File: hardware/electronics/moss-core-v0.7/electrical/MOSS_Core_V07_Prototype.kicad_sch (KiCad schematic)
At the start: 0 parts

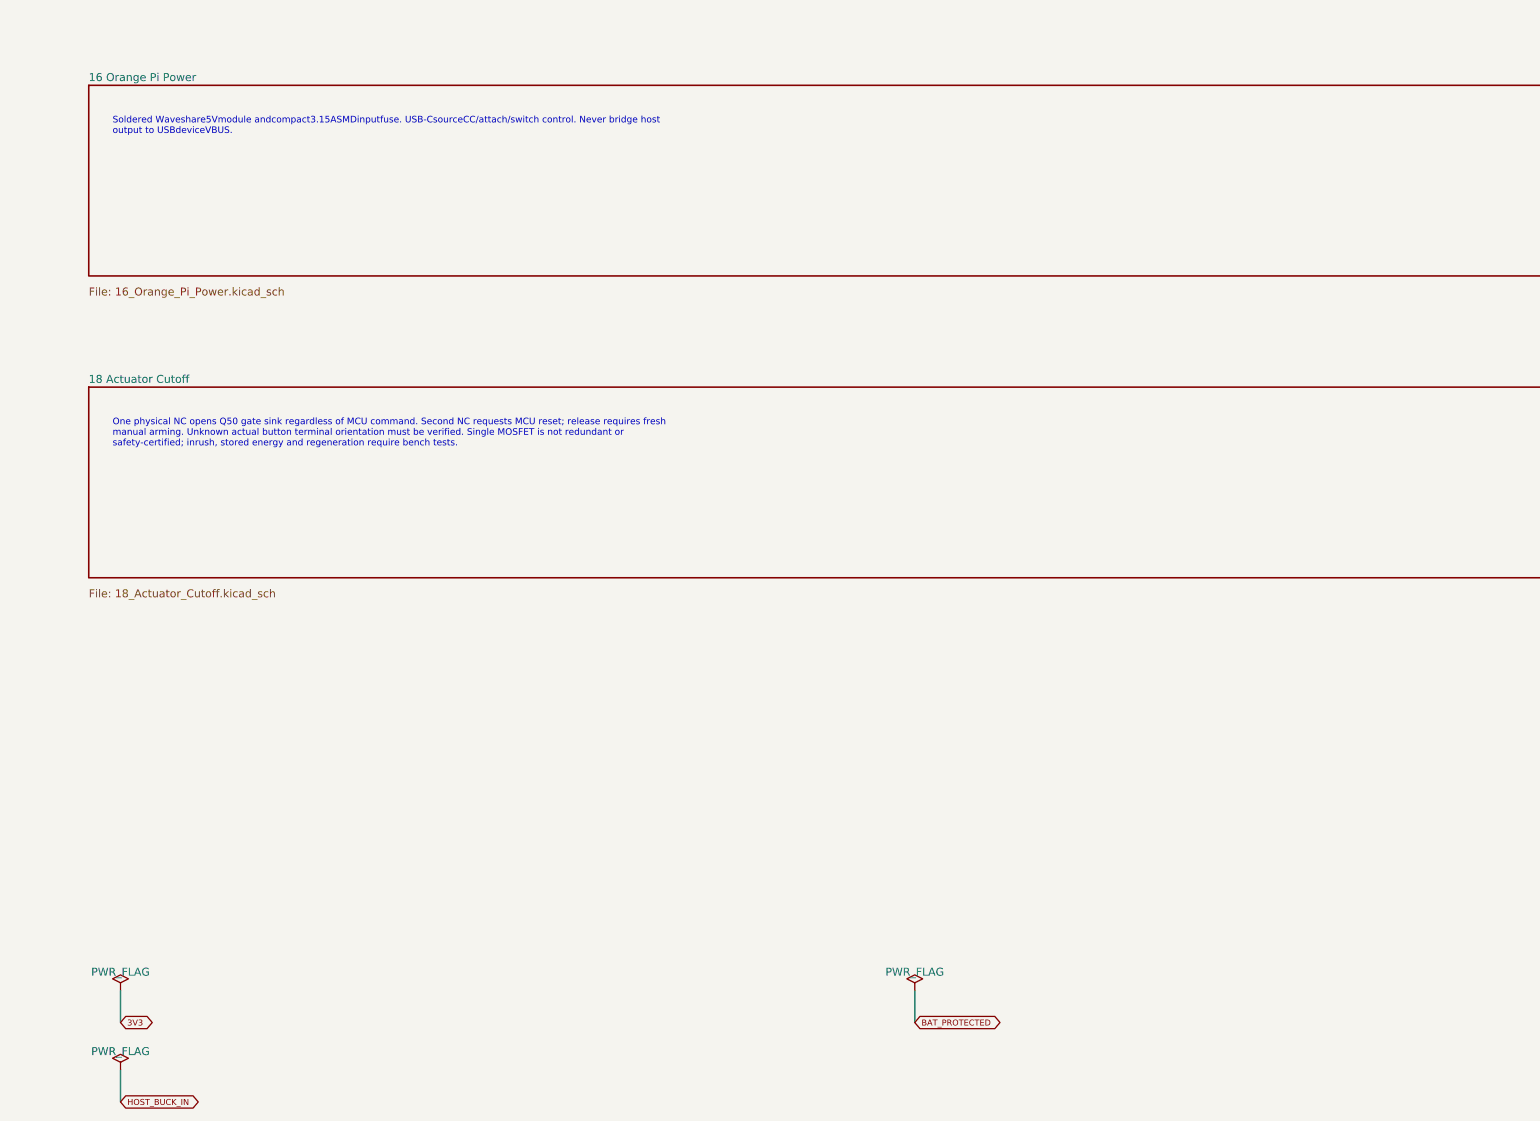
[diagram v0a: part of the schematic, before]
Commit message: Update MOSS Core V0.7 prototype files for 31 October
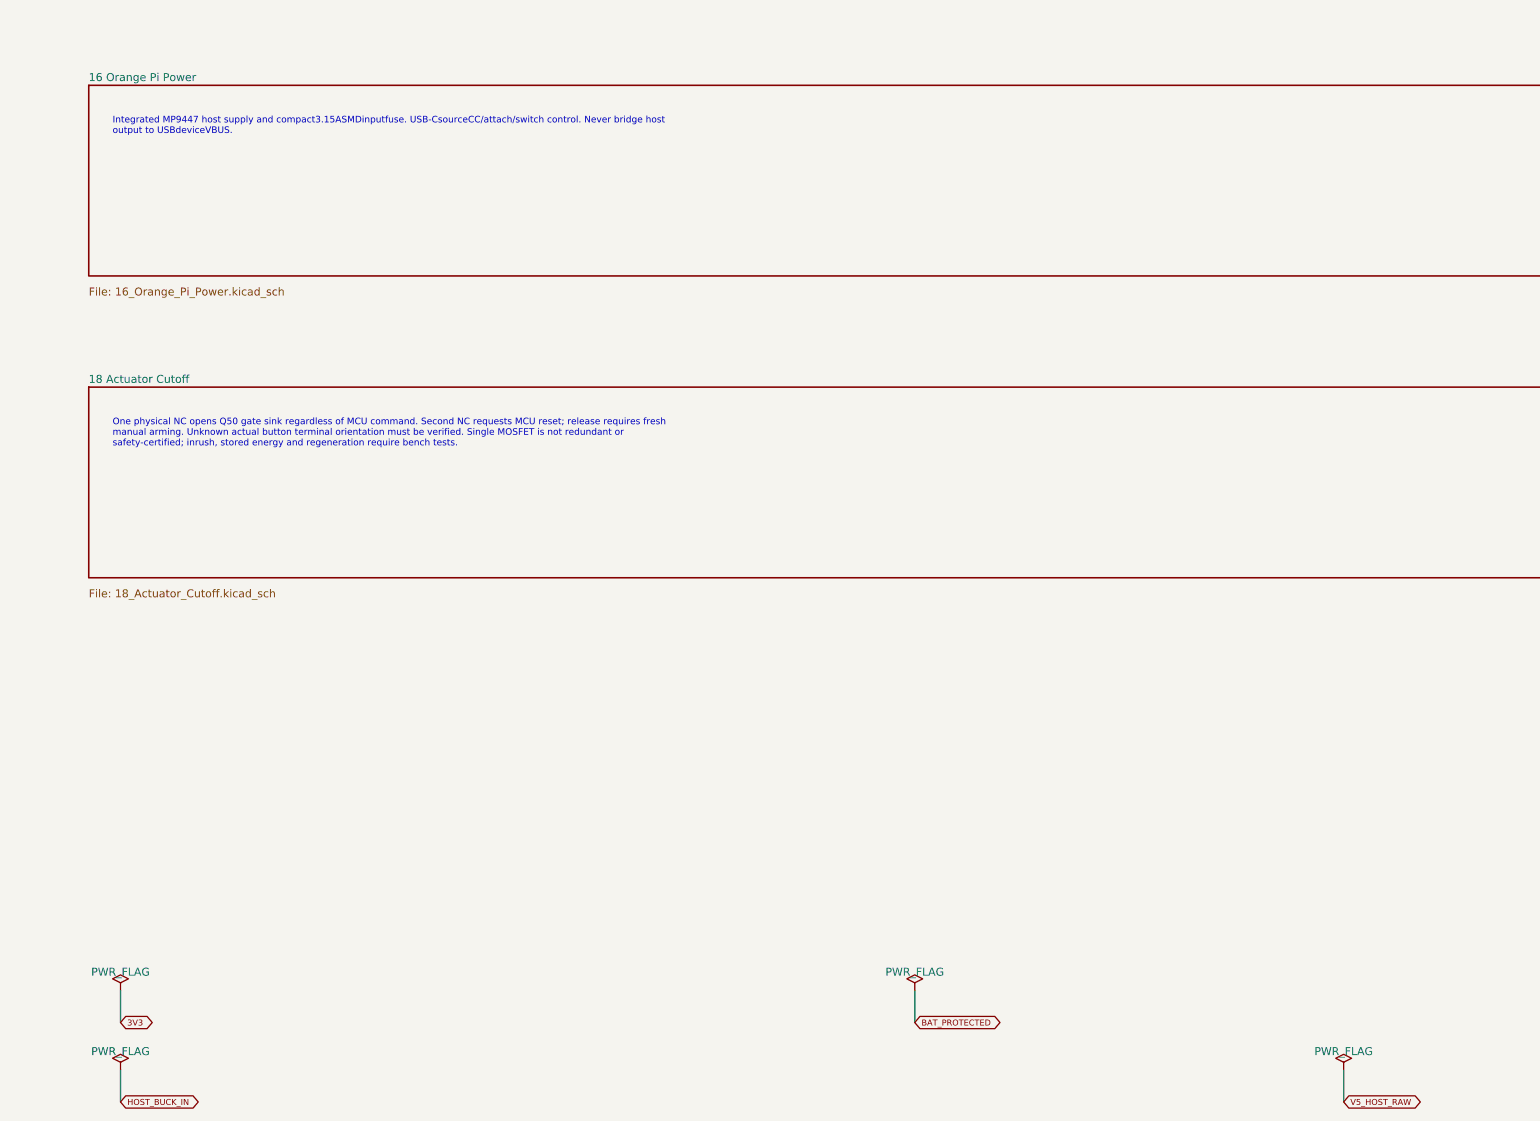
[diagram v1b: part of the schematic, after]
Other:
- note added: "Integrated MP9447 host supply and compact3.15ASMDinputfuse. USB-CsourceCC/attach/switch control. Never bridge host output to USBdeviceVBUS."
- note removed: "Soldered Waveshare5Vmodule andcompact3.15ASMDinputfuse. USB-CsourceCC/attach/switch control. Never bridge host output to USBdeviceVBUS."
